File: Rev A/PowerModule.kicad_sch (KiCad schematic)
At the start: 107 parts, among them J1 NC6-P108-02, J2 NC6-P108-02, J3 1x7 Socket P2.54mm, K1 Relay_SPDT, Q1 IRLZ44N, Q2 IRLZ44N, Q3 IRLZ44N, U1 LM324, U2 LM324, U3 LM7805

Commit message: cleaned up routing
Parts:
- added TP11: TestPoint_Small, TestPoint:TestPoint_Pad_D2.0mm, symbol Connector:TestPoint_Small
- J1, J2: footprint TerminalBlock_MetzConnect:TerminalBlock_MetzConnect_Type703_RT10N02HGLU_1x02_P9.52mm_Horizontal -> Connectors_SurgicalLighting:NC6-P108-02
- K1: value Relay_SPDT -> PC792A-1C-C-12S-DN-X
- R20: value 10K -> 330R
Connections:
- net 12V_Lights: now also D11.2 (A), D8.2 (A); no longer R30.1, R35.1
- net GND_Lights1: now also R30.2; no longer D8.1 (K)
- net GND_Lights2: now also R35.2; no longer D11.1 (K)
- net RelaySelectHighPreference: now also TP11.1
- net RelayFETGate: now reaches C1.1, Q1.1 (G), R1.2, R2.1
- net RELAY_COIL_N: now reaches D14.1 (K), D2.2 (A), K1.85, Q1.2 (D)
- new net: D8.1 (K), R30.1
- new net: D11.1 (K), R35.1
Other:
- note added: "Rg"
- note added: "Shunt: 5mV/A Amplifier: 61.6x Output: 0.308V/A"
- moved on the sheet: D11, D8, R30, R35
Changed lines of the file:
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@@
 	)
 	(junction
+		(at 194.31 66.04)
+		(diameter 0)
+		(color 0 0 0 0)
+	)
+	(junction
 		(at 222.25 73.66)
 		(diameter 0)
@@
 	(wire
 		(pts
+			(xy 194.31 66.04) (xy 199.39 66.04)
+		)
+		(stroke
+			(width 0)
+			(type default)
+		)
+	)
+	(wire
+		(pts
 			(xy 161.29 99.06) (xy 165.1 99.06)
 		)
@@
 	(wire
 		(pts
+			(xy 194.31 64.77) (xy 194.31 66.04)
+		)
+		(stroke
+			(width 0)
+			(type default)
+		)
+	)
+	(wire
+		(pts
 			(xy 46.99 45.72) (xy 49.53 45.72)
 		)
@@
 	(wire
 		(pts
+			(xy 213.36 59.69) (xy 222.25 59.69)
+		)
+		(stroke
+			(width 0)
+			(type default)
+		)
+	)
+	(wire
+		(pts
 			(xy 83.82 149.86) (xy 83.82 151.13)
 		)
@@
 	(wire
 		(pts
-			(xy 213.36 59.69) (xy 222.25 59.69)
-		)
-		(stroke
-			(width 0)
-			(type default)
-		)
-	)
-	(wire
-		(pts
 			(xy 182.88 107.95) (xy 182.88 101.6)
 		)
@@
 	(wire
 		(pts
-			(xy 185.42 66.04) (xy 199.39 66.04)
+			(xy 185.42 66.04) (xy 194.31 66.04)
 		)
 		(stroke
@@
 		)
 	)
+	(text "Shunt: 5mV/A\nAmplifier: 61.6x\nOutput: 0.308V/A"
+		(exclude_from_sim no)
+		(at 136.398 139.954 0)
+		(effects
+			(font
+				(size 1.27 1.27)
+			)
+		)
+	)
 	(text "Light Set 1 PWM Control"
 		(exclude_from_sim no)
@@
 		)
 	)
+	(text "Rg"
+		(exclude_from_sim no)
+		(at 78.232 153.67 0)
+		(effects
+			(font
+				(size 1.27 1.27)
+			)
+		)
+	)
 	(label "ISense2_P"
 		(at 57.15 167.64 0)
@@
 		)
 	)
+	(label "RelayFETGate"
+		(at 205.74 66.04 0)
+		(fields_autoplaced yes)
+		(effects
+			(font
+				(size 0.8 0.8)
+			)
+			(justify left bottom)
+		)
+	)
 	(label "VIN_OPA_PWR"
 		(at 101.6 66.04 0)
@@
 		)
 	)
+	(label "RELAY_COIL_N"
+		(at 198.12 59.69 0)
+		(fields_autoplaced yes)
+		(effects
+			(font
+				(size 1.27 1.27)
+			)
+			(justify left bottom)
+		)
+	)
 	(label "ISense2_P"
 		(at 78.74 99.06 0)
@@
 			)
 		)
-		(property "Footprint" "TerminalBlock_MetzConnect:TerminalBlock_MetzConnect_Type703_RT10N02HGLU_1x02_P9.52mm_Horizontal"
+		(property "Footprint" "Connectors_SurgicalLighting:NC6-P108-02"
 			(at 260.35 110.49 0)
 			(effects
@@
 		(fields_autoplaced yes)
 		(property "Reference" "K1"
-			(at 238.76 49.53 0)
+			(at 238.76 48.9585 0)
 			(effects
 				(font
@@
 			)
 		)
-		(property "Value" "Relay_SPDT"
-			(at 238.76 52.07 0)
+		(property "Value" "PC792A-1C-C-12S-DN-X"
+			(at 238.76 51.4985 0)
 			(effects
 				(font
@@
 	(symbol
 		(lib_id "Device:LED_Small")
-		(at 228.6 115.57 90)
+		(at 228.6 107.95 90)
 		(unit 1)
 		(exclude_from_sim no)
@@
 		(dnp no)
 		(property "Reference" "D8"
-			(at 224.536 114.046 90)
+			(at 224.536 106.426 90)
 			(effects
 				(font
@@
 		)
 		(property "Value" "LED WHITE"
-			(at 219.964 115.57 90)
+			(at 219.964 107.95 90)
 			(effects
 				(font
@@
 		)
 		(property "Footprint" "LED_SMD:LED_0805_2012Metric"
-			(at 228.6 115.57 90)
+			(at 228.6 107.95 90)
 			(effects
 				(font
@@
 		)
 		(property "Datasheet" "~"
-			(at 228.6 115.57 90)
+			(at 228.6 107.95 90)
 			(effects
 				(font
@@
 		)
 		(property "Description" "Light emitting diode, small symbol"
-			(at 228.6 115.57 0)
+			(at 228.6 107.95 0)
 			(effects
 				(font
@@
 		(dnp no)
 		(property "Reference" "R20"
-			(at 83.82 154.432 90)
+			(at 83.82 154.686 90)
 			(effects
 				(font
@@
 			)
 		)
-		(property "Value" "10K"
-			(at 80.264 153.67 0)
+		(property "Value" "330R"
+			(at 79.502 153.67 0)
 			(effects
 				(font
@@
 	(symbol
 		(lib_id "Device:LED_Small")
-		(at 114.3 115.57 90)
+		(at 114.3 107.95 90)
 		(unit 1)
 		(exclude_from_sim no)
@@
 		(dnp no)
 		(property "Reference" "D11"
-			(at 109.728 114.046 90)
+			(at 109.728 106.426 90)
 			(effects
 				(font
@@
 		)
 		(property "Value" "LED WHITE"
-			(at 105.918 115.57 90)
+			(at 105.918 107.95 90)
 			(effects
 				(font
@@
 		)
 		(property "Footprint" "LED_SMD:LED_0805_2012Metric"
-			(at 114.3 115.57 90)
+			(at 114.3 107.95 90)
 			(effects
 				(font
@@
 		)
 		(property "Datasheet" "~"
-			(at 114.3 115.57 90)
+			(at 114.3 107.95 90)
 			(effects
 				(font
@@
 		)
 		(property "Description" "Light emitting diode, small symbol"
-			(at 114.3 115.57 0)
+			(at 114.3 107.95 0)
 			(effects
 				(font
@@
 	(symbol
 		(lib_id "jlcpcb-basic-resistor:0805,10k")
-		(at 114.3 107.95 0)
+		(at 114.3 115.57 0)
 		(unit 1)
 		(exclude_from_sim no)
@@
 		(dnp no)
 		(property "Reference" "R35"
-			(at 114.3 109.22 90)
+			(at 114.3 116.84 90)
 			(effects
 				(font
@@
 		)
 		(property "Value" "0805,10k"
-			(at 107.442 107.95 0)
+			(at 107.442 115.57 0)
 			(effects
 				(font
@@
 		)
 		(property "Footprint" "Resistor_SMD:R_0805_2012Metric"
-			(at 114.3 107.95 0)
+			(at 114.3 115.57 0)
 			(effects
 				(font
@@
 		)
 		(property "Datasheet" "https://datasheet.lcsc.com/lcsc/2110251730_UNI-ROYAL-Uniroyal-Elec-0805W8F1002T5E_C17414.pdf"
-			(at 114.3 107.95 0)
+			(at 114.3 115.57 0)
 			(effects
 				(font
@@
 		)
 		(property "Description" "1% 1 8W Thick Film Resistors 150V   100ppm    -55    155   10k   0805 Chip Resistor - Surface Mount ROHS"
-			(at 114.3 107.95 0)
+			(at 114.3 115.57 0)
 			(effects
 				(font
@@
 		)
 		(property "LCSC" "C17414"
-			(at 114.3 107.95 0)
+			(at 114.3 115.57 0)
 			(effects
 				(font
@@
 		)
 		(property "MFG" "UNI-ROYAL(Uniroyal Elec)"
-			(at 114.3 107.95 0)
+			(at 114.3 115.57 0)
 			(effects
 				(font
@@
 		)
 		(property "MFGPN" "0805W8F1002T5E"
-			(at 114.3 107.95 0)
+			(at 114.3 115.57 0)
 			(effects
 				(font
@@
 	(symbol
 		(lib_id "Connector:TestPoint_Small")
+		(at 194.31 64.77 0)
+		(unit 1)
+		(exclude_from_sim yes)
+		(in_bom no)
+		(on_board yes)
+		(dnp no)
+		(property "Reference" "TP11"
+			(at 192.278 63.246 0)
+			(effects
+				(font
+					(size 0.8 0.8)
+				)
+				(justify left)
+			)
+		)
+		(property "Value" "TestPoint_Small"
+			(at 195.58 66.0399 0)
+			(effects
+				(font
+					(size 0.8 0.8)
+				)
+				(justify left)
+				(hide yes)
+			)
+		)
+		(property "Footprint" "TestPoint:TestPoint_Pad_D2.0mm"
+			(at 199.39 64.77 0)
+			(effects
+				(font
+					(size 1.27 1.27)
+				)
+				(hide yes)
+			)
+		)
+		(property "Datasheet" "~"
+			(at 199.39 64.77 0)
+			(effects
+				(font
+					(size 1.27 1.27)
+				)
+				(hide yes)
+			)
+		)
+		(property "Description" "test point"
+			(at 194.31 64.77 0)
+			(effects
+				(font
+					(size 1.27 1.27)
+				)
+				(hide yes)
+			)
+		)
+		(pin "1"
+		)
+		(instances
+			(project "PowerModule"
+				(path "/352d7abe-fc72-4473-8b68-62eecf44f496"
+					(reference "TP11")
+					(unit 1)
+				)
+			)
+		)
+	)
+	(symbol
+		(lib_id "Connector:TestPoint_Small")
 		(at 168.91 167.64 0)
 		(unit 1)
@@
 			)
 		)
-		(property "Footprint" "TerminalBlock_MetzConnect:TerminalBlock_MetzConnect_Type703_RT10N02HGLU_1x02_P9.52mm_Horizontal"
+		(property "Footprint" "Connectors_SurgicalLighting:NC6-P108-02"
 			(at 146.05 110.49 0)
 			(effects
@@
 	(symbol
 		(lib_id "jlcpcb-basic-resistor:0805,10k")
-		(at 228.6 107.95 0)
+		(at 228.6 115.57 0)
 		(unit 1)
 		(exclude_from_sim no)
@@
 		(dnp no)
 		(property "Reference" "R30"
-			(at 228.6 109.22 90)
+			(at 228.6 116.84 90)
 			(effects
 				(font
@@
 		)
 		(property "Value" "0805,10k"
-			(at 221.742 107.95 0)
+			(at 221.742 115.57 0)
 			(effects
 				(font
@@
 		)
 		(property "Footprint" "Resistor_SMD:R_0805_2012Metric"
-			(at 228.6 107.95 0)
+			(at 228.6 115.57 0)
 			(effects
 				(font
@@
 		)
 		(property "Datasheet" "https://datasheet.lcsc.com/lcsc/2110251730_UNI-ROYAL-Uniroyal-Elec-0805W8F1002T5E_C17414.pdf"
-			(at 228.6 107.95 0)
+			(at 228.6 115.57 0)
 			(effects
 				(font
@@
 		)
 		(property "Description" "1% 1 8W Thick Film Resistors 150V   100ppm    -55    155   10k   0805 Chip Resistor - Surface Mount ROHS"
-			(at 228.6 107.95 0)
+			(at 228.6 115.57 0)
 			(effects
 				(font
@@
 		)
 		(property "LCSC" "C17414"
-			(at 228.6 107.95 0)
+			(at 228.6 115.57 0)
 			(effects
 				(font
@@
 		)
 		(property "MFG" "UNI-ROYAL(Uniroyal Elec)"
-			(at 228.6 107.95 0)
+			(at 228.6 115.57 0)
 			(effects
 				(font
@@
 		)
 		(property "MFGPN" "0805W8F1002T5E"
-			(at 228.6 107.95 0)
+			(at 228.6 115.57 0)
 			(effects
 				(font

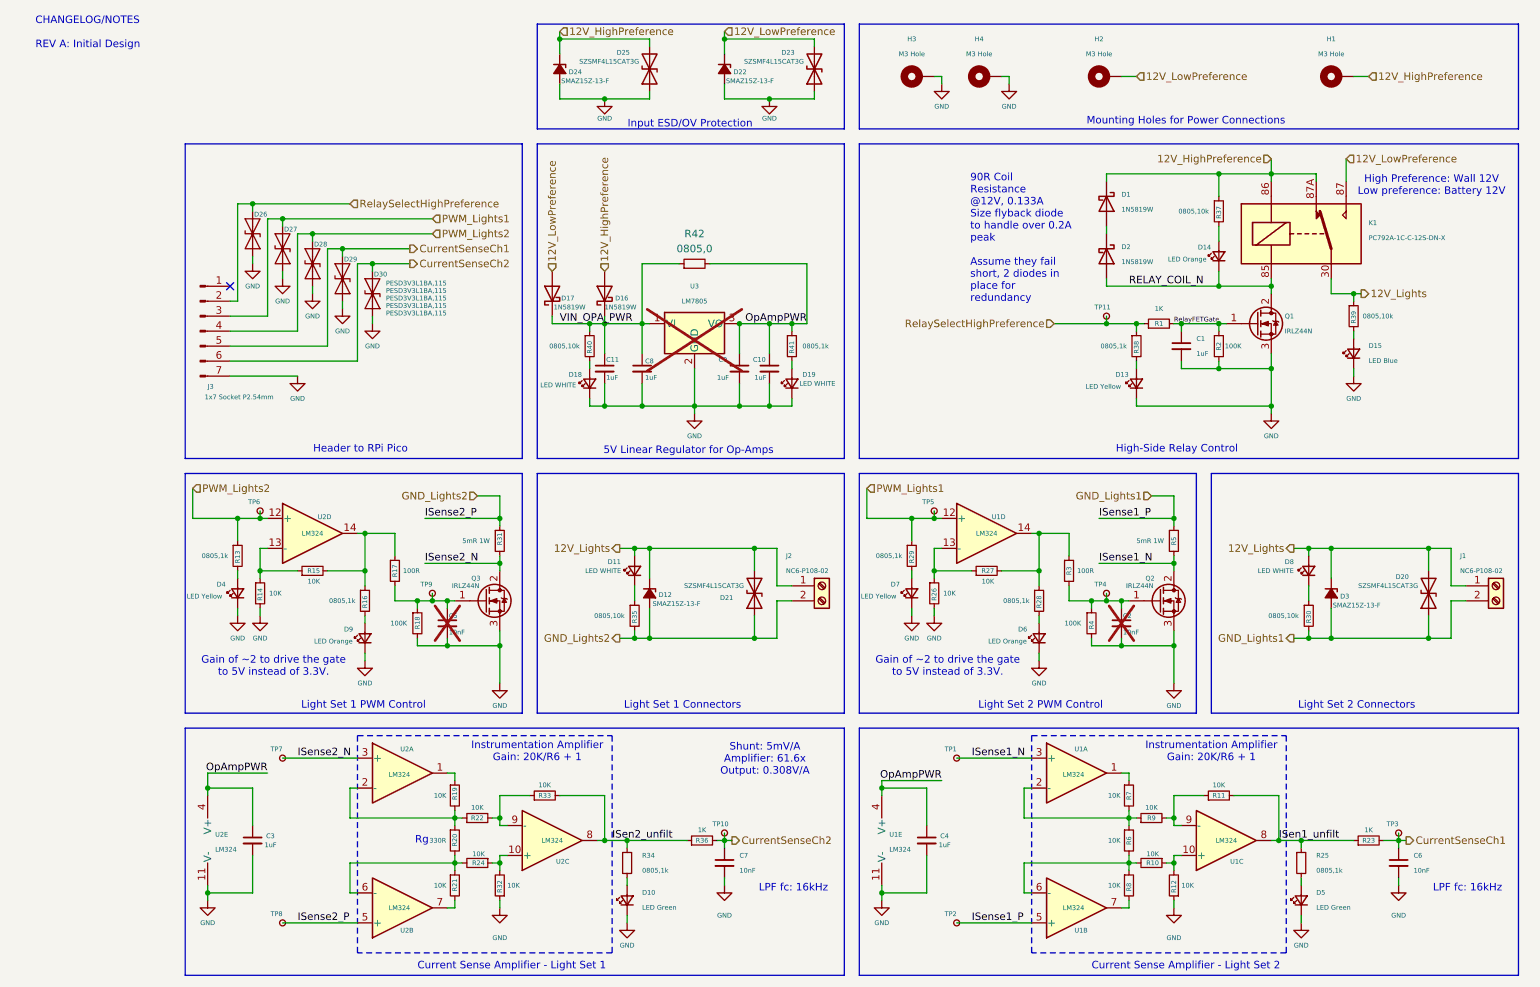
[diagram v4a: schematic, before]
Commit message: updated screw terminal
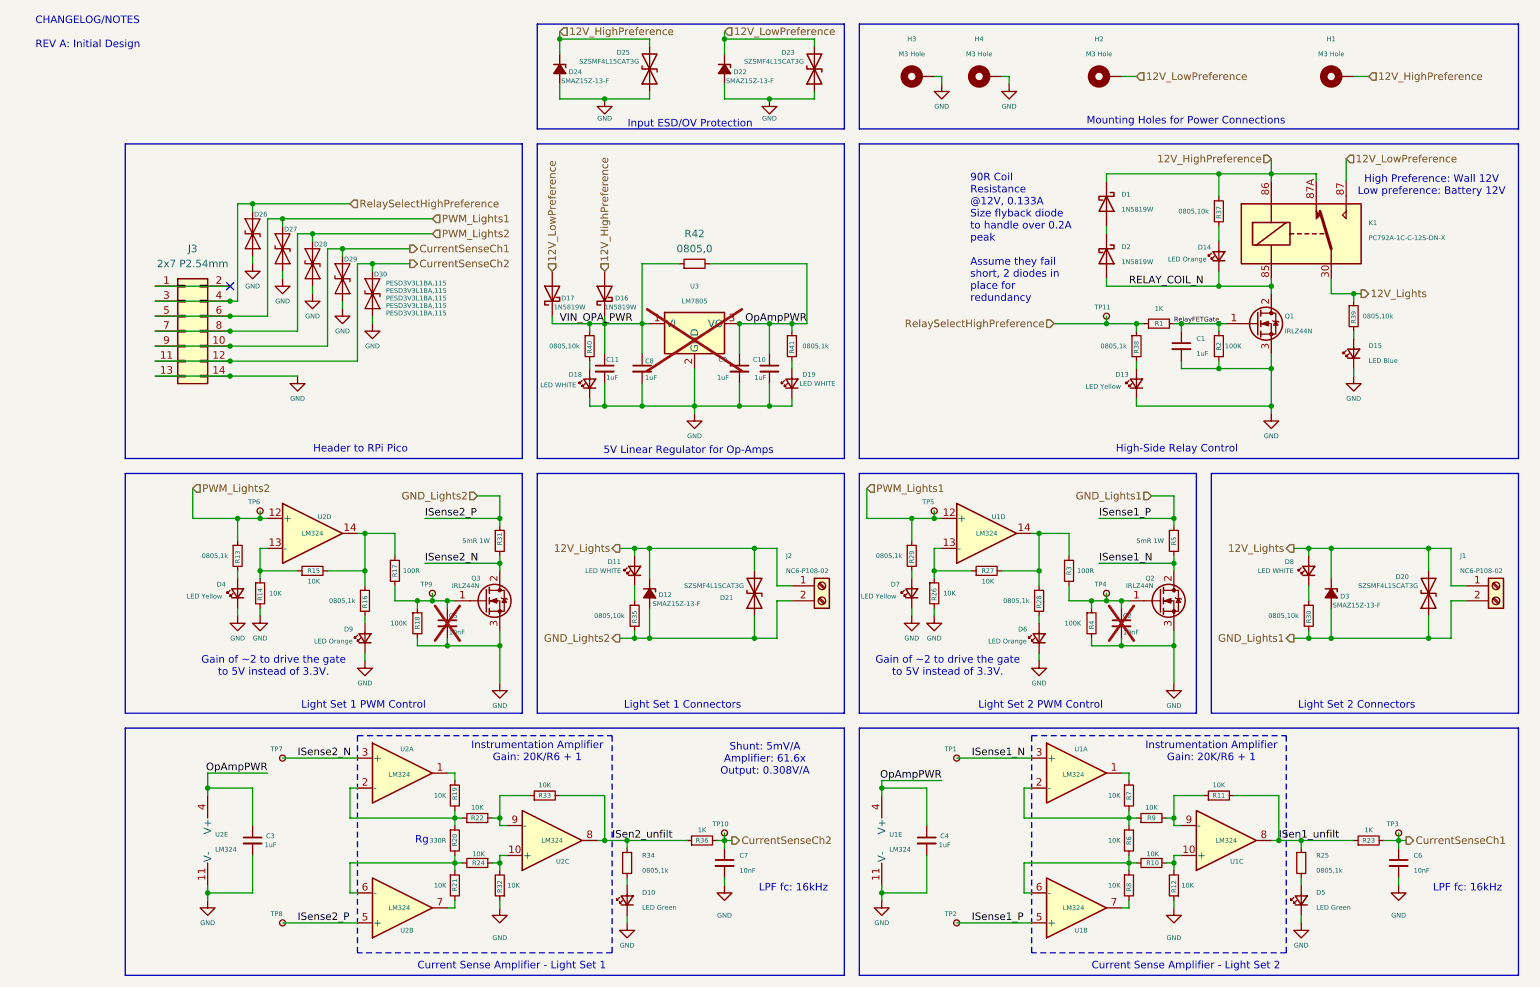
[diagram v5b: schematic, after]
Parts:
- removed J3: 1x7 Socket P2.54mm, Connector_PinSocket_2.54mm:PinSocket_1x07_P2.54mm_Vertical, symbol Connector:Conn_01x07_Pin
- added J3: 2x7 P2.54mm, Connector_PinHeader_2.54mm:PinHeader_2x07_P2.54mm_Vertical, symbol Connector_Generic:Conn_02x07_Odd_Even
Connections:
- net CurrentSenseCh1: now also J3.10 (Pin_10), J3.9 (Pin_9)
- net CurrentSenseCh2: now also J3.11 (Pin_11), J3.12 (Pin_12)
- net GND: now also J3.13 (Pin_13), J3.14 (Pin_14)
- net PWM_Lights1: now also J3.5 (Pin_5), J3.6 (Pin_6)
- net PWM_Lights2: now also J3.7 (Pin_7), J3.8 (Pin_8)
- net RelaySelectHighPreference: now also J3.3 (Pin_3), J3.4 (Pin_4)
- new net: J3.1 (Pin_1), J3.2 (Pin_2)
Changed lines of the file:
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@@
 	)
 	(junction
+		(at 45.72 67.31)
+		(diameter 0)
+		(color 0 0 0 0)
+	)
+	(junction
 		(at 91.44 120.65)
 		(diameter 0)
@@
 	)
 	(junction
+		(at 45.72 69.85)
+		(diameter 0)
+		(color 0 0 0 0)
+	)
+	(junction
 		(at 165.1 99.06)
 		(diameter 0)
@@
 	)
 	(junction
+		(at 45.72 62.23)
+		(diameter 0)
+		(color 0 0 0 0)
+	)
+	(junction
 		(at 129.54 153.67)
 		(diameter 0)
@@
 	)
 	(junction
+		(at 45.72 72.39)
+		(diameter 0)
+		(color 0 0 0 0)
+	)
+	(junction
 		(at 196.85 120.65)
 		(diameter 0)
@@
 	)
 	(junction
+		(at 45.72 74.93)
+		(diameter 0)
+		(color 0 0 0 0)
+	)
+	(junction
 		(at 205.74 106.68)
 		(diameter 0)
@@
 	)
 	(junction
+		(at 45.72 64.77)
+		(diameter 0)
+		(color 0 0 0 0)
+	)
+	(junction
 		(at 109.22 80.01)
 		(diameter 0)
@@
 	(wire
 		(pts
+			(xy 33.02 62.23) (xy 45.72 62.23)
+		)
+		(stroke
+			(width 0)
+			(type default)
+		)
+	)
+	(wire
+		(pts
 			(xy 156.21 143.51) (xy 166.37 143.51)
 		)
@@
 	(wire
 		(pts
+			(xy 33.02 64.77) (xy 45.72 64.77)
+		)
+		(stroke
+			(width 0)
+			(type default)
+		)
+	)
+	(wire
+		(pts
 			(xy 165.1 104.14) (xy 166.37 104.14)
 		)
@@
 	(wire
 		(pts
+			(xy 33.02 59.69) (xy 45.72 59.69)
+		)
+		(stroke
+			(width 0)
+			(type default)
+		)
+	)
+	(wire
+		(pts
 			(xy 129.54 17.78) (xy 144.78 17.78)
 		)
@@
 	(wire
 		(pts
+			(xy 33.02 72.39) (xy 45.72 72.39)
+		)
+		(stroke
+			(width 0)
+			(type default)
+		)
+	)
+	(wire
+		(pts
 			(xy 91.44 106.68) (xy 91.44 107.95)
 		)
@@
 	(wire
 		(pts
+			(xy 33.02 67.31) (xy 45.72 67.31)
+		)
+		(stroke
+			(width 0)
+			(type default)
+		)
+	)
+	(wire
+		(pts
 			(xy 41.91 163.83) (xy 41.91 162.56)
 		)
@@
 	(wire
 		(pts
+			(xy 33.02 69.85) (xy 45.72 69.85)
+		)
+		(stroke
+			(width 0)
+			(type default)
+		)
+	)
+	(wire
+		(pts
 			(xy 129.54 160.02) (xy 129.54 161.29)
 		)
@@
 	(wire
 		(pts
+			(xy 33.02 74.93) (xy 45.72 74.93)
+		)
+		(stroke
+			(width 0)
+			(type default)
+		)
+	)
+	(wire
+		(pts
 			(xy 180.34 149.86) (xy 198.12 149.86)
 		)
@@
 	)
 	(rectangle
-		(start 38.1 134.62)
+		(start 27.94 134.62)
 		(end 149.86 176.53)
 		(stroke
@@
 	)
 	(rectangle
-		(start 38.1 35.56)
+		(start 27.94 35.56)
 		(end 95.25 88.9)
 		(stroke
@@
 	)
 	(rectangle
-		(start 38.1 91.44)
+		(start 27.94 91.44)
 		(end 95.25 132.08)
 		(stroke
@@
 	)
 	(symbol
+		(lib_id "Connector_Generic:Conn_02x07_Odd_Even")
+		(at 38.1 67.31 0)
+		(unit 1)
+		(exclude_from_sim no)
+		(in_bom yes)
+		(on_board yes)
+		(dnp no)
+		(fields_autoplaced yes)
+		(property "Reference" "J3"
+			(at 39.37 53.34 0)
+			(effects
+				(font
+					(size 1.27 1.27)
+				)
+			)
+		)
+		(property "Value" "2x7 P2.54mm"
+			(at 39.37 55.88 0)
+			(effects
+				(font
+					(size 1.27 1.27)
+				)
+			)
+		)
+		(property "Footprint" "Connector_PinHeader_2.54mm:PinHeader_2x07_P2.54mm_Vertical"
+			(at 38.1 67.31 0)
+			(effects
+				(font
+					(size 1.27 1.27)
+				)
+				(hide yes)
+			)
+		)
+		(property "Datasheet" "~"
+			(at 38.1 67.31 0)
+			(effects
+				(font
+					(size 1.27 1.27)
+				)
+				(hide yes)
+			)
+		)
+		(property "Description" "Generic connector, double row, 02x07, odd/even pin numbering scheme (row 1 odd numbers, row 2 even numbers), script generated (kicad-library-utils/schlib/autogen/connector/)"
+			(at 38.1 67.31 0)
+			(effects
+				(font
+					(size 1.27 1.27)
+				)
+				(hide yes)
+			)
+		)
+		(pin "13"
+		)
+		(pin "7"
+		)
+		(pin "11"
+		)
+		(pin "4"
+		)
+		(pin "9"
+		)
+		(pin "12"
+		)
+		(pin "14"
+		)
+		(pin "6"
+		)
+		(pin "1"
+		)
+		(pin "3"
+		)
+		(pin "2"
+		)
+		(pin "5"
+		)
+		(pin "10"
+		)
+		(pin "8"
+		)
+		(instances
+			(project "PowerModule"
+				(path "/352d7abe-fc72-4473-8b68-62eecf44f496"
+					(reference "J3")
+					(unit 1)
+				)
+			)
+		)
+	)
+	(symbol
 		(lib_name "GND_1")
 		(lib_id "power:GND")
@@
 					(unit 1)
 				)
-			)
-		)
-	)
-	(symbol
-		(lib_id "Connector:Conn_01x07_Pin")
-		(at 40.64 67.31 0)
-		(unit 1)
-		(exclude_from_sim no)
-		(in_bom yes)
-		(on_board yes)
-		(dnp no)
-		(property "Reference" "J3"
-			(at 42.418 76.708 0)
-			(effects
-				(font
-					(size 0.8 0.8)
-				)
-			)
-		)
-		(property "Value" "1x7 Socket P2.54mm"
-			(at 47.244 78.486 0)
-			(effects
-				(font
-					(size 0.8 0.8)
-				)
-			)
-		)
-		(property "Footprint" "Connector_PinSocket_2.54mm:PinSocket_1x07_P2.54mm_Vertical"
-			(at 40.64 67.31 0)
-			(effects
-				(font
-					(size 1.27 1.27)
-				)
-				(hide yes)
-			)
-		)
-		(property "Datasheet" "~"
-			(at 40.64 67.31 0)
-			(effects
-				(font
-					(size 1.27 1.27)
-				)
-				(hide yes)
-			)
-		)
-		(property "Description" "Generic connector, single row, 01x07, script generated"
-			(at 40.64 67.31 0)
-			(effects
-				(font
-					(size 1.27 1.27)
-				)
-				(hide yes)
-			)
-		)
-		(pin "5"
-		)
-		(pin "1"
-		)
-		(pin "2"
-		)
-		(pin "7"
-		)
-		(pin "6"
-		)
-		(pin "3"
-		)
-		(pin "4"
-		)
-		(instances
-			(project "PowerModule"
-				(path "/352d7abe-fc72-4473-8b68-62eecf44f496"
-					(reference "J3")
-					(unit 1)
-				)
